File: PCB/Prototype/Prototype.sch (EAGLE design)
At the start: 1 part

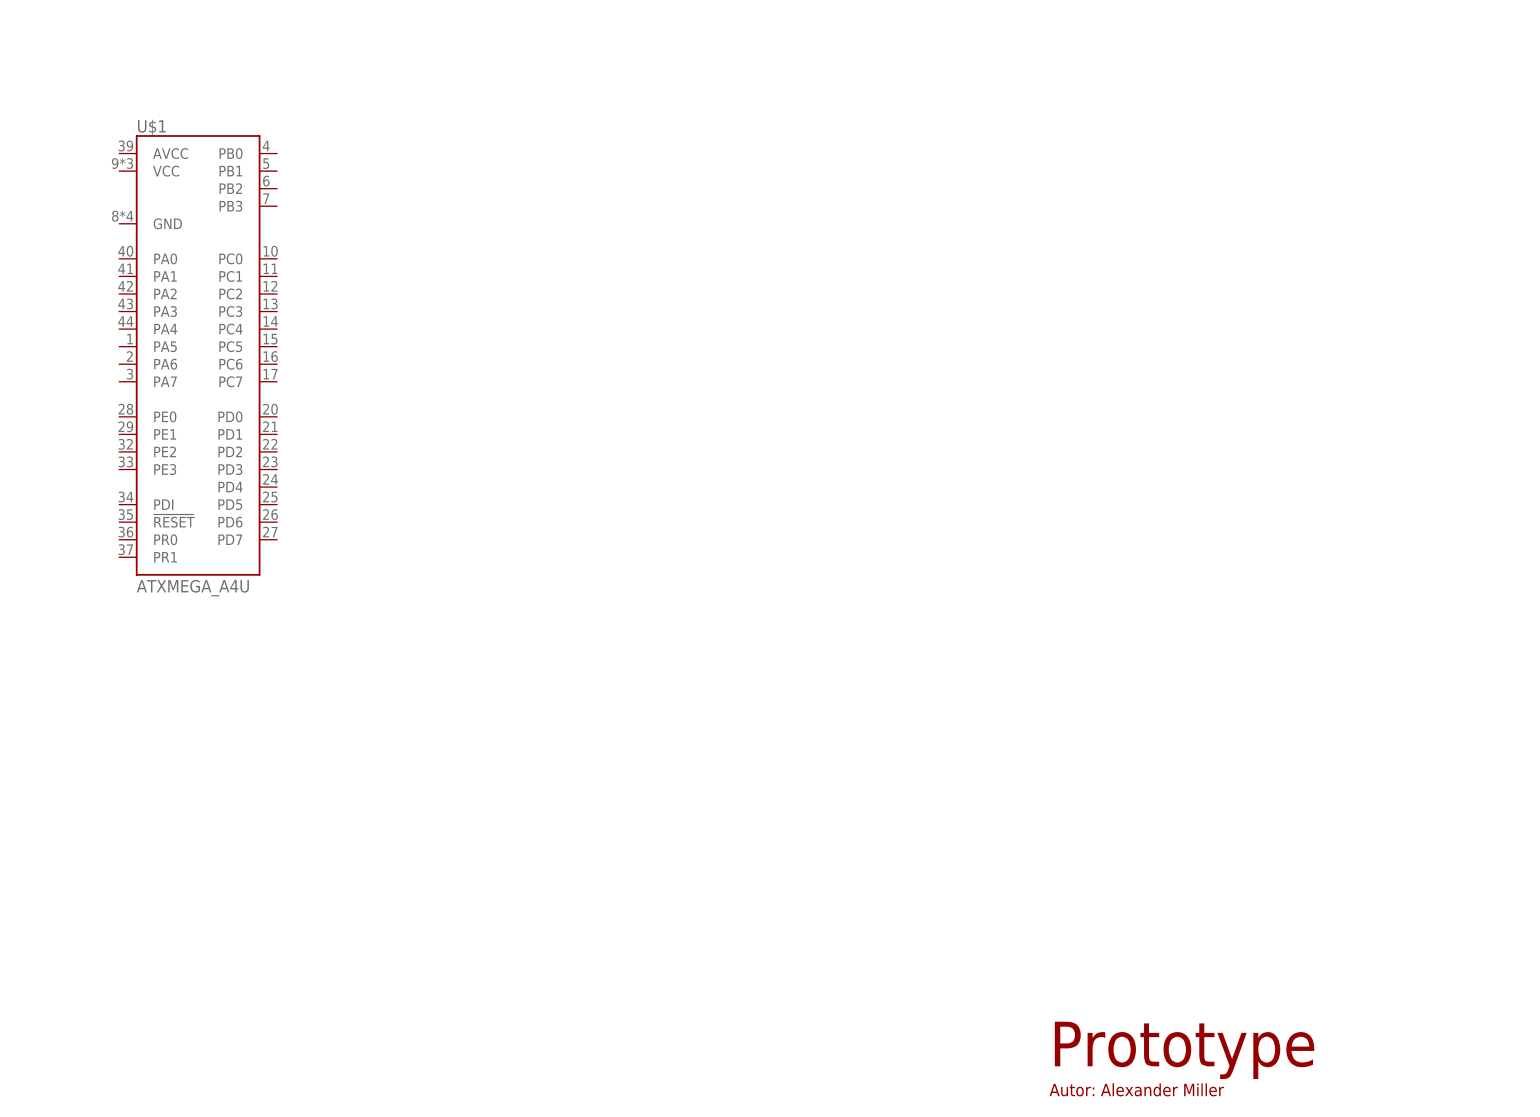
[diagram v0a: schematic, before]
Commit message: Upload Gamepad
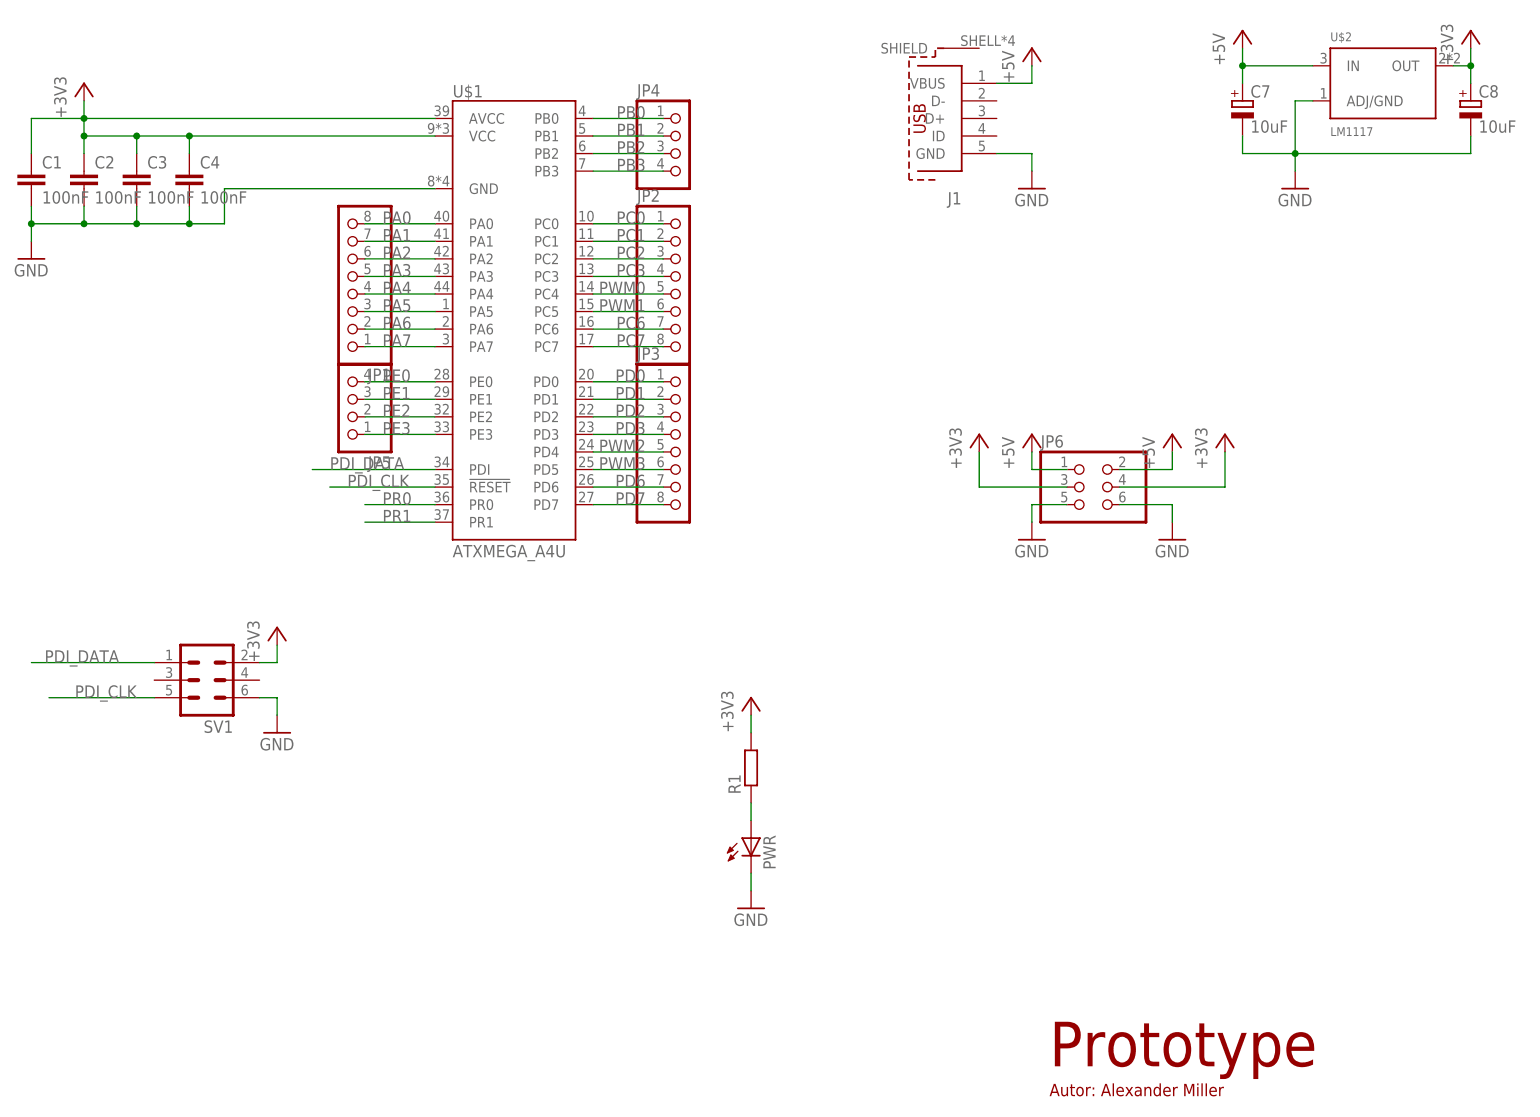
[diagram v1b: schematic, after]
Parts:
- added C1, C2, C3, C4: 100nF, rcl:C-EUC0805
- added C7, C8: 10uF, rcl:CPOL-EUSMCP
- added J1: (no value), InputOutputIO (rev18a):629105136821
- added JP1, JP2, JP3: (no value), pinhead:PINHD-1X8
- added JP4, JP5: (no value), pinhead:PINHD-1X4
- added JP6: (no value), pinhead:PINHD-2X3
- added PWR: (no value), led:LEDSML0805
- added R1: (no value), rcl:R-EU_R0805
- added SV1: (no value), con-ml:ML6
- added U$2: LM1117, RPI:LM1117
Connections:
- new net +3V3: C1.1, C2.1, C3.1, C4.1, C8.+, JP6.3, JP6.4, R1.2, SV1.2, U$1.AVCC, U$1.VCC, U$2.OUT
- new net +5V: C7.+, J1.VBUS, JP6.1, JP6.2, U$2.IN
- new net GND: C1.2, C2.2, C3.2, C4.2, C7.-, C8.-, J1.GND, JP6.5, JP6.6, PWR.C, SV1.6, U$1.GND, U$2.ADJ/GND
- new net N$1: PWR.A, R1.1
- new net PA0: JP1.8, U$1.PA0
- new net PA1: JP1.7, U$1.PA1
- new net PA2: JP1.6, U$1.PA2
- new net PA3: JP1.5, U$1.PA3
- new net PA4: JP1.4, U$1.PA4
- new net PA5: JP1.3, U$1.PA5
- new net PA6: JP1.2, U$1.PA6
- new net PA7: JP1.1, U$1.PA7
- new net PB0: JP4.1, U$1.PB0
- new net PB1: JP4.2, U$1.PB1
- new net PB2: JP4.3, U$1.PB2
- new net PB3: JP4.4, U$1.PB3
- new net PC0: JP2.1, U$1.PC0
- new net PC1: JP2.2, U$1.PC1
- new net PC2: JP2.3, U$1.PC2
- new net PC3: JP2.4, U$1.PC3
- new net PC6: JP2.7, U$1.PC6
- new net PC7: JP2.8, U$1.PC7
- new net PD0: JP3.1, U$1.PD0
- new net PD1: JP3.2, U$1.PD1
- new net PD2: JP3.3, U$1.PD2
- new net PD3: JP3.4, U$1.PD3
- new net PD6: JP3.7, U$1.PD6
- new net PD7: JP3.8, U$1.PD7
- new net PDI_CLK: SV1.5, U$1.!RESET
- new net PDI_DATA: SV1.1, U$1.PDI
- new net PE0: JP5.4, U$1.PE0
- new net PE1: JP5.3, U$1.PE1
- new net PE2: JP5.2, U$1.PE2
- new net PE3: JP5.1, U$1.PE3
- new net PR0: U$1.PR0
- new net PR1: U$1.PR1
- new net PWM0: JP2.5, U$1.PC4
- new net PWM1: JP2.6, U$1.PC5
- new net PWM2: JP3.5, U$1.PD4
- new net PWM3: JP3.6, U$1.PD5
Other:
- moved on the sheet: U$1
